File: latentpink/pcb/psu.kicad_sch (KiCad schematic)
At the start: 110 parts, among them J13 CONN_01X05, J14 CONN_01X03, J6 BARREL_JACK, U10 MYMGK1R812ERSR, U11 MYMGK00504ERSR, U12 STM32L031-QFN32, U13 MYMGK00504ERSR, U14 MYMGK00504ERSR, U15 MYMGK00504ERSR, U16 NCP45521IMNTWG-H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

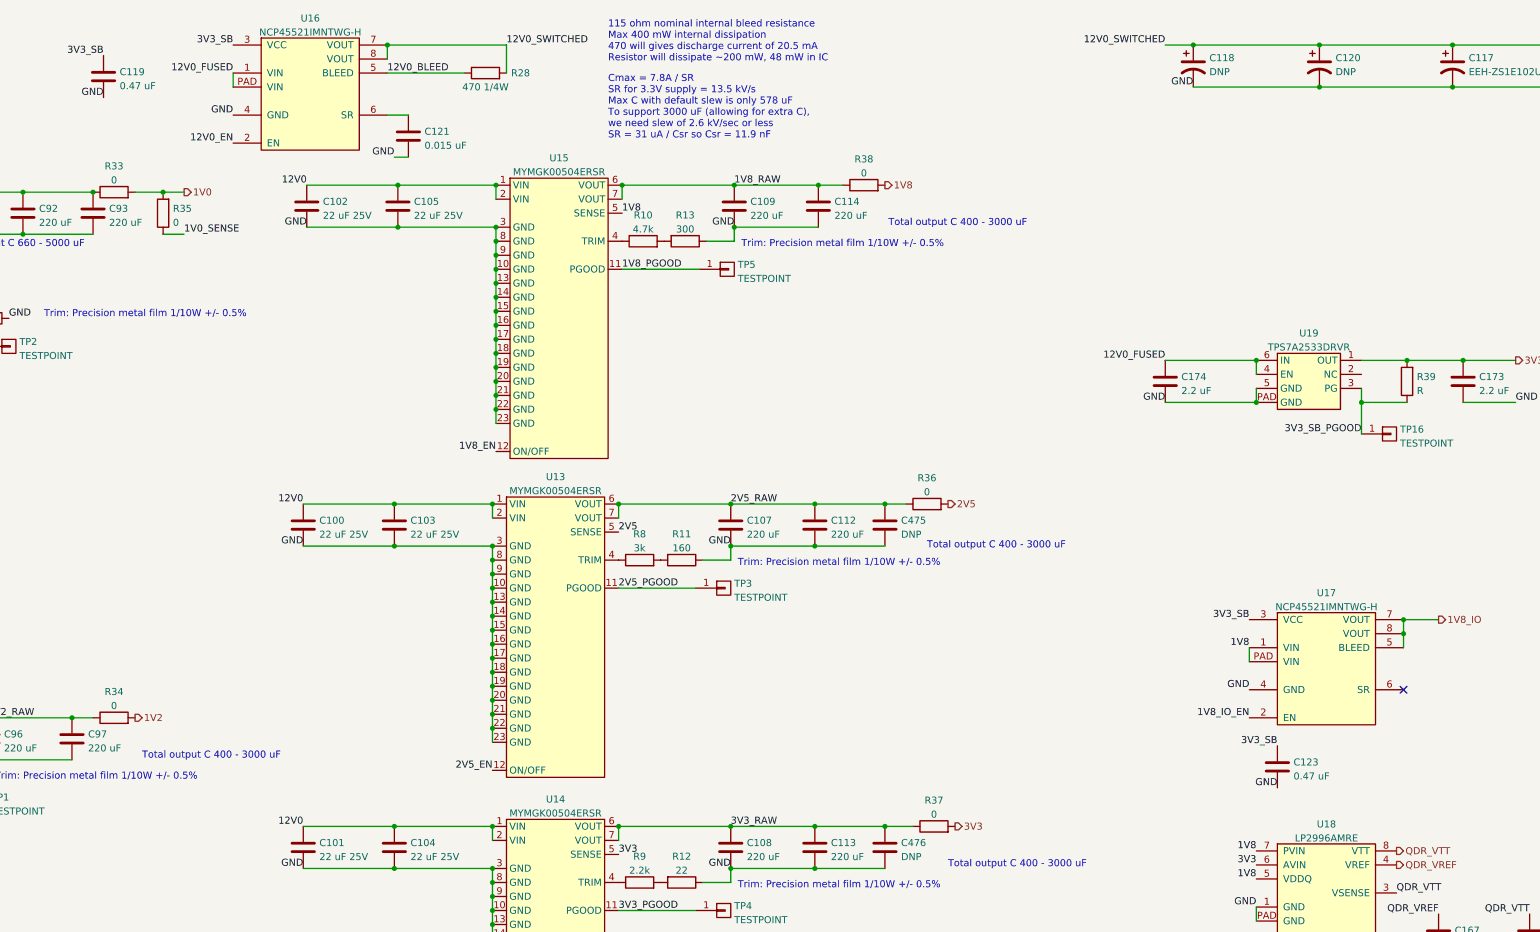
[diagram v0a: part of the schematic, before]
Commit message: Finished initial schematic, ready for design review
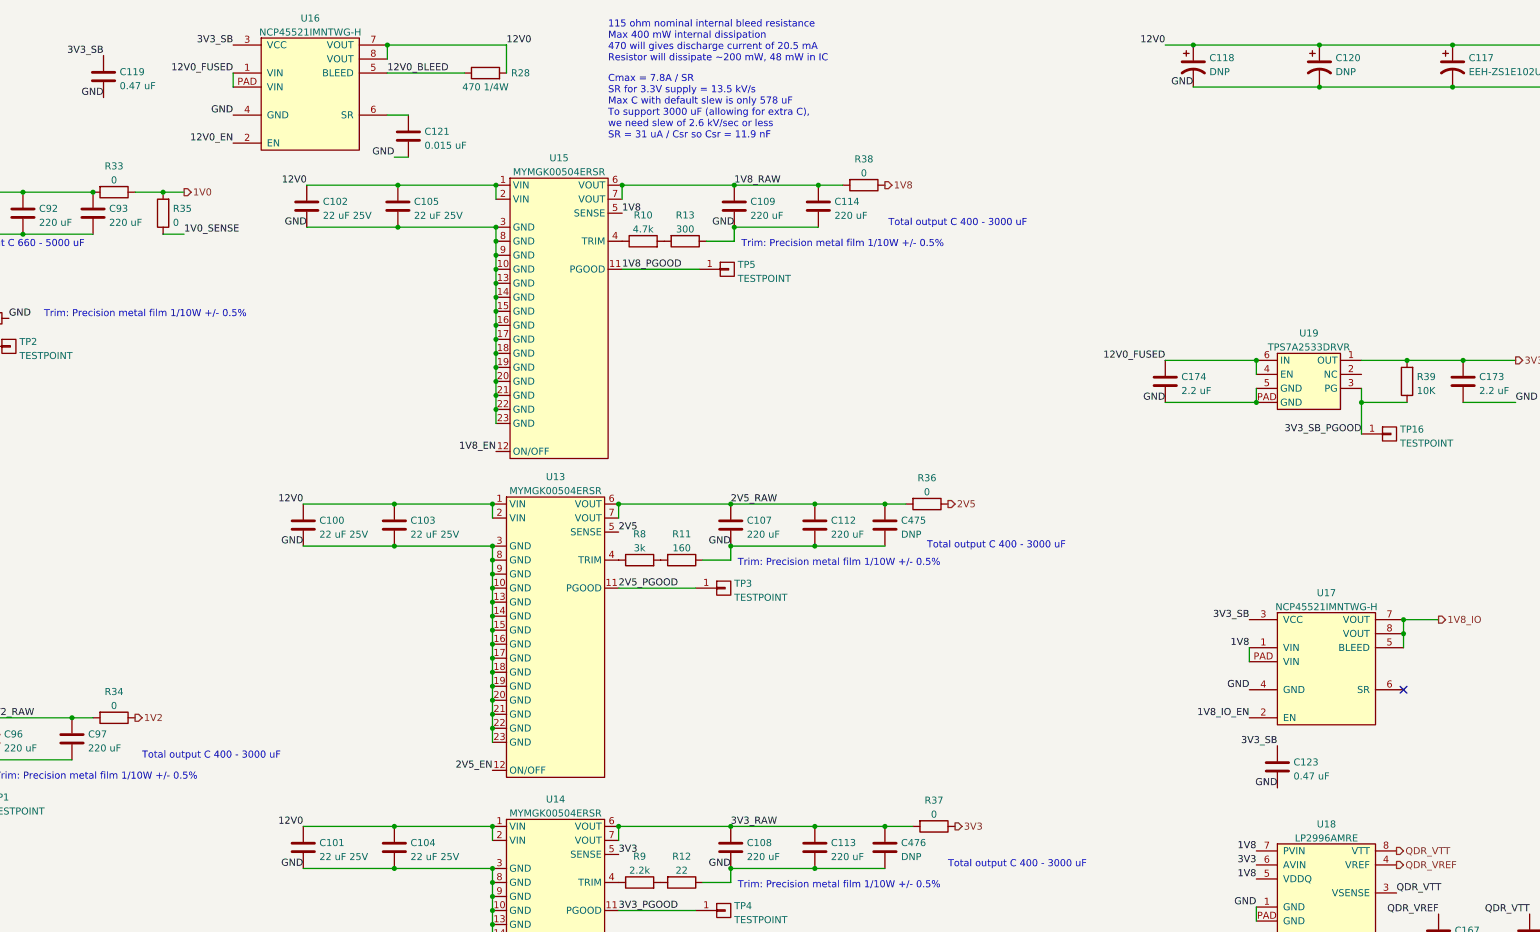
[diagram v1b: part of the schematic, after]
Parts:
- C169: footprint (none) -> azonenberg_pcb:EIA_1206_CAP_NOSILK
- C171: footprint (none) -> azonenberg_pcb:EIA_1210_CAP_NOSILK
- C173, C174: footprint (none) -> azonenberg_pcb:EIA_0805_CAP_NOSILK
- R1, R11, R12, R13, R8, R9: footprint (none) -> azonenberg_pcb:EIA_0402_RES_NOSILK
- R33, R34, R36, R37, R38: symbol device:R -> passive-azonenberg:R_PWR
- R39: value R -> 10K; footprint (none) -> azonenberg_pcb:EIA_0402_RES_NOSILK
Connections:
- net 1V0: now also R33.1; no longer R33.2
- net 1V0_RAW: now also R33.2; no longer R33.1
- net 1V2: now also R34.1; no longer R34.2
- net 1V2_RAW: now also R34.2; no longer R34.1
- net 1V8: now also R38.1; no longer R38.2
- net 1V8_RAW: now also R38.2; no longer R38.1
- net 2V5: now also R36.1; no longer R36.2
- net 2V5_RAW: now also R36.2; no longer R36.1
- net 3V3: now also R37.1; no longer R37.2
- net 3V3_RAW: now also R37.2; no longer R37.1
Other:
- moved on the sheet: R33, R34, R36, R37, R38
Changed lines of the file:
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@@
   (junction (at 236.22 245.11) (diameter 0) (color 0 0 0 0)
   )
-  (junction (at 116.84 45.72) (diameter 0) (color 0 0 0 0)
-  )
   (junction (at 189.23 127.635) (diameter 0) (color 0 0 0 0)
   )
@@
   (junction (at 104.14 45.72) (diameter 0) (color 0 0 0 0)
   )
+  (junction (at 116.84 45.72) (diameter 0) (color 0 0 0 0)
+  )
   (junction (at 54.61 48.26) (diameter 0) (color 0 0 0 0)
   )
@@
     (effects (font (size 1.27 1.27)) (justify right bottom))
   )
-  (label "12V0_SWITCHED" (at 311.15 19.05 180)
+  (label "12V0" (at 311.15 19.05 180)
     (effects (font (size 1.27 1.27)) (justify right bottom))
   )
@@
     (effects (font (size 1.27 1.27)) (justify left bottom))
   )
-  (label "12V0_SWITCHED" (at 191.77 19.05 0)
+  (label "12V0" (at 191.77 19.05 0)
     (effects (font (size 1.27 1.27)) (justify left bottom))
   )
@@
       (effects (font (size 1.27 1.27)) (justify left))
     )
-    (property "Footprint" "" (id 2) (at 366.0902 83.82 0)
+    (property "Footprint" "azonenberg_pcb:EIA_0805_CAP_NOSILK" (id 2) (at 366.0902 83.82 0)
       (effects (font (size 1.27 1.27)) hide)
     )
@@
     (property "Reference" "R13" (id 0) (at 224.155 49.8942 90))
     (property "Value" "300" (id 1) (at 224.155 52.4311 90))
-    (property "Footprint" "" (id 2) (at 224.155 52.832 90)
+    (property "Footprint" "azonenberg_pcb:EIA_0402_RES_NOSILK" (id 2) (at 224.155 52.832 90)
       (effects (font (size 1.27 1.27)) hide)
     )
@@
     (pin "2")
   )
-  (symbol (lib_id "device:R") (at 256.54 44.45 90) (unit 1)
+  (symbol (lib_id "passive-azonenberg:R_PWR") (at 256.54 44.45 270) (unit 1)
     (in_bom yes) (on_board yes) (fields_autoplaced)
     (property "Reference" "R38" (id 0) (at 256.54 39.7342 90))
     (property "Value" "0" (id 1) (at 256.54 42.2711 90))
-    (property "Footprint" "azonenberg_pcb:EIA_0402_RES_NOSILK" (id 2) (at 256.54 46.228 90)
+    (property "Footprint" "azonenberg_pcb:EIA_0402_RES_NOSILK" (id 2) (at 256.54 42.672 90)
       (effects (font (size 1.27 1.27)) hide)
     )
@@
     (property "Reference" "R8" (id 0) (at 215.9 107.6792 90))
     (property "Value" "3k" (id 1) (at 215.9 110.2161 90))
-    (property "Footprint" "" (id 2) (at 215.9 114.173 90)
+    (property "Footprint" "azonenberg_pcb:EIA_0402_RES_NOSILK" (id 2) (at 215.9 114.173 90)
       (effects (font (size 1.27 1.27)) hide)
     )
@@
       (effects (font (size 1.27 1.27)) (justify left))
     )
-    (property "Footprint" "" (id 2) (at 361.6452 196.85 0)
+    (property "Footprint" "azonenberg_pcb:EIA_1210_CAP_NOSILK" (id 2) (at 361.6452 196.85 0)
       (effects (font (size 1.27 1.27)) hide)
     )
@@
       (effects (font (size 1.27 1.27)) (justify left))
     )
-    (property "Footprint" "" (id 2) (at 312.1152 83.82 0)
+    (property "Footprint" "azonenberg_pcb:EIA_0805_CAP_NOSILK" (id 2) (at 312.1152 83.82 0)
       (effects (font (size 1.27 1.27)) hide)
     )
@@
     (property "Reference" "R11" (id 0) (at 223.52 107.6792 90))
     (property "Value" "160" (id 1) (at 223.52 110.2161 90))
-    (property "Footprint" "" (id 2) (at 223.52 110.617 90)
+    (property "Footprint" "azonenberg_pcb:EIA_0402_RES_NOSILK" (id 2) (at 223.52 110.617 90)
       (effects (font (size 1.27 1.27)) hide)
     )
@@
     (property "Reference" "R9" (id 0) (at 215.9 166.0992 90))
     (property "Value" "2.2k" (id 1) (at 215.9 168.6361 90))
-    (property "Footprint" "" (id 2) (at 215.9 172.593 90)
+    (property "Footprint" "azonenberg_pcb:EIA_0402_RES_NOSILK" (id 2) (at 215.9 172.593 90)
       (effects (font (size 1.27 1.27)) hide)
     )
@@
     (pin "2")
   )
-  (symbol (lib_id "device:R") (at 267.97 102.235 90) (unit 1)
+  (symbol (lib_id "passive-azonenberg:R_PWR") (at 267.97 102.235 270) (unit 1)
     (in_bom yes) (on_board yes) (fields_autoplaced)
     (property "Reference" "R36" (id 0) (at 267.97 97.5192 90))
     (property "Value" "0" (id 1) (at 267.97 100.0561 90))
-    (property "Footprint" "azonenberg_pcb:EIA_0402_RES_NOSILK" (id 2) (at 267.97 104.013 90)
+    (property "Footprint" "azonenberg_pcb:EIA_0402_RES_NOSILK" (id 2) (at 267.97 100.457 90)
       (effects (font (size 1.27 1.27)) hide)
     )
@@
       (effects (font (size 1.27 1.27)) (justify right))
     )
-    (property "Value" "R" (id 1) (at 356.743 81.7122 0)
+    (property "Value" "10K" (id 1) (at 356.743 81.7122 0)
       (effects (font (size 1.27 1.27)) (justify right))
     )
-    (property "Footprint" "" (id 2) (at 356.743 80.01 90)
+    (property "Footprint" "azonenberg_pcb:EIA_0402_RES_NOSILK" (id 2) (at 356.743 80.01 90)
       (effects (font (size 1.27 1.27)) hide)
     )
@@
     (pin "2")
   )
-  (symbol (lib_id "device:R") (at 120.65 140.97 90) (unit 1)
+  (symbol (lib_id "passive-azonenberg:R_PWR") (at 120.65 140.97 270) (unit 1)
     (in_bom yes) (on_board yes) (fields_autoplaced)
     (property "Reference" "R34" (id 0) (at 120.65 136.2542 90))
     (property "Value" "0" (id 1) (at 120.65 138.7911 90))
-    (property "Footprint" "azonenberg_pcb:EIA_0402_RES_NOSILK" (id 2) (at 120.65 142.748 90)
+    (property "Footprint" "azonenberg_pcb:EIA_0402_RES_NOSILK" (id 2) (at 120.65 139.192 90)
       (effects (font (size 1.27 1.27)) hide)
     )
@@
     (pin "2")
   )
-  (symbol (lib_id "device:R") (at 269.24 160.655 90) (unit 1)
+  (symbol (lib_id "passive-azonenberg:R_PWR") (at 269.24 160.655 270) (unit 1)
     (in_bom yes) (on_board yes) (fields_autoplaced)
     (property "Reference" "R37" (id 0) (at 269.24 155.9392 90))
     (property "Value" "0" (id 1) (at 269.24 158.4761 90))
-    (property "Footprint" "azonenberg_pcb:EIA_0402_RES_NOSILK" (id 2) (at 269.24 162.433 90)
+    (property "Footprint" "azonenberg_pcb:EIA_0402_RES_NOSILK" (id 2) (at 269.24 158.877 90)
       (effects (font (size 1.27 1.27)) hide)
     )
@@
     (pin "2")
   )
-  (symbol (lib_id "power-azonenberg:MYMGK00504ERSR") (at 192.405 93.98 0) (unit 1)
+  (symbol (lib_name "MYMGK00504ERSR_3") (lib_id "power-azonenberg:MYMGK00504ERSR") (at 192.405 93.98 0) (unit 1)
     (in_bom yes) (on_board yes)
     (property "Reference" "U15" (id 0) (at 201.295 39.531 0))
@@
     (pin "2")
   )
-  (symbol (lib_id "power-azonenberg:MYMGK00504ERSR") (at 191.77 151.765 0) (unit 1)
+  (symbol (lib_name "MYMGK00504ERSR_2") (lib_id "power-azonenberg:MYMGK00504ERSR") (at 191.77 151.765 0) (unit 1)
     (in_bom yes) (on_board yes)
     (property "Reference" "U13" (id 0) (at 200.66 97.316 0))
@@
     (pin "PAD")
   )
-  (symbol (lib_id "device:R") (at 120.65 45.72 90) (unit 1)
+  (symbol (lib_id "passive-azonenberg:R_PWR") (at 120.65 45.72 270) (unit 1)
     (in_bom yes) (on_board yes) (fields_autoplaced)
     (property "Reference" "R33" (id 0) (at 120.65 41.0042 90))
     (property "Value" "0" (id 1) (at 120.65 43.5411 90))
-    (property "Footprint" "azonenberg_pcb:EIA_0402_RES_NOSILK" (id 2) (at 120.65 47.498 90)
+    (property "Footprint" "azonenberg_pcb:EIA_0402_RES_NOSILK" (id 2) (at 120.65 43.942 90)
       (effects (font (size 1.27 1.27)) hide)
     )
@@
     (pin "2")
   )
-  (symbol (lib_id "power-azonenberg:MYMGK00504ERSR") (at 57.15 190.5 0) (unit 1)
+  (symbol (lib_name "MYMGK00504ERSR_1") (lib_id "power-azonenberg:MYMGK00504ERSR") (at 57.15 190.5 0) (unit 1)
     (in_bom yes) (on_board yes)
     (property "Reference" "U11" (id 0) (at 66.04 136.051 0))
@@
     (property "Reference" "R1" (id 0) (at 90.17 63.8642 90))
     (property "Value" "16K" (id 1) (at 90.17 66.4011 90))
-    (property "Footprint" "" (id 2) (at 90.17 70.358 90)
+    (property "Footprint" "azonenberg_pcb:EIA_0402_RES_NOSILK" (id 2) (at 90.17 70.358 90)
       (effects (font (size 1.27 1.27)) hide)
     )
@@
       (effects (font (size 1.27 1.27)) (justify left))
     )
-    (property "Footprint" "" (id 2) (at 310.8452 196.85 0)
+    (property "Footprint" "azonenberg_pcb:EIA_1206_CAP_NOSILK" (id 2) (at 310.8452 196.85 0)
       (effects (font (size 1.27 1.27)) hide)
     )
@@
     (property "Reference" "R12" (id 0) (at 223.52 166.0992 90))
     (property "Value" "22" (id 1) (at 223.52 168.6361 90))
-    (property "Footprint" "" (id 2) (at 223.52 169.037 90)
+    (property "Footprint" "azonenberg_pcb:EIA_0402_RES_NOSILK" (id 2) (at 223.52 169.037 90)
       (effects (font (size 1.27 1.27)) hide)
     )

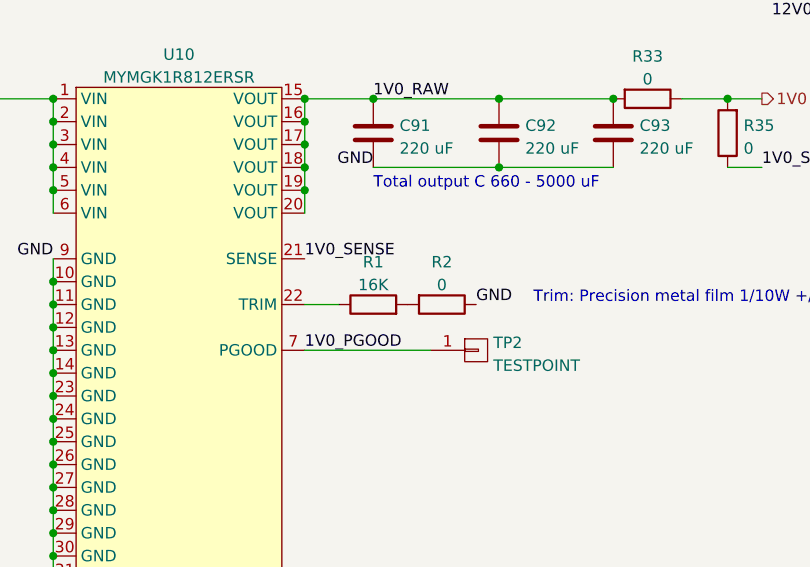
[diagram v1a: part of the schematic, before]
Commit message: Added some debug LEDs, PMOD, and temp sensors
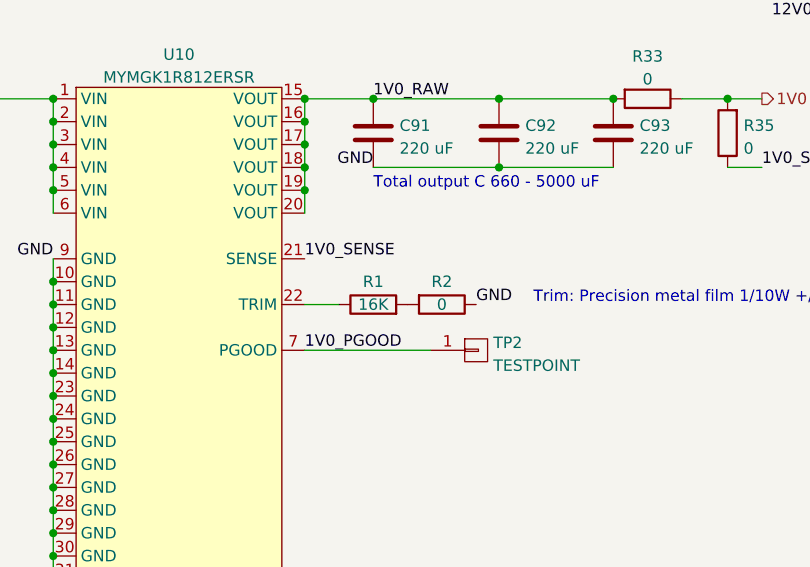
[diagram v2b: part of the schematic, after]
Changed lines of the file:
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@@
   )
   (symbol (lib_id "device:R") (at 97.79 68.58 270) (unit 1)
-    (in_bom yes) (on_board yes) (fields_autoplaced)
-    (property "Reference" "R2" (id 0) (at 97.79 63.8642 90))
-    (property "Value" "0" (id 1) (at 97.79 66.4011 90))
+    (in_bom yes) (on_board yes)
+    (property "Reference" "R2" (id 0) (at 97.79 66.04 90))
+    (property "Value" "0" (id 1) (at 97.79 68.58 90))
     (property "Footprint" "azonenberg_pcb:EIA_0402_RES_NOSILK" (id 2) (at 97.79 66.802 90)
       (effects (font (size 1.27 1.27)) hide)
@@
   )
   (symbol (lib_id "device:R") (at 90.17 68.58 90) (unit 1)
-    (in_bom yes) (on_board yes) (fields_autoplaced)
-    (property "Reference" "R1" (id 0) (at 90.17 63.8642 90))
-    (property "Value" "16K" (id 1) (at 90.17 66.4011 90))
+    (in_bom yes) (on_board yes)
+    (property "Reference" "R1" (id 0) (at 90.17 66.04 90))
+    (property "Value" "16K" (id 1) (at 90.17 68.58 90))
     (property "Footprint" "azonenberg_pcb:EIA_0402_RES_NOSILK" (id 2) (at 90.17 70.358 90)
       (effects (font (size 1.27 1.27)) hide)
